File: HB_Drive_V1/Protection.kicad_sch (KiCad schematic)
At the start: 48 parts, among them J701 Conn_02x02_Odd_Even, J702 Conn_02x02_Odd_Even, SW701 PTS636SL43SMTRLFS, SW704 PTS636SL43SMTRLFS, U402 74LS08, U701 74AUC2G02, U702 74LS32, U703 TL082, U704 TL082, U705 LM311

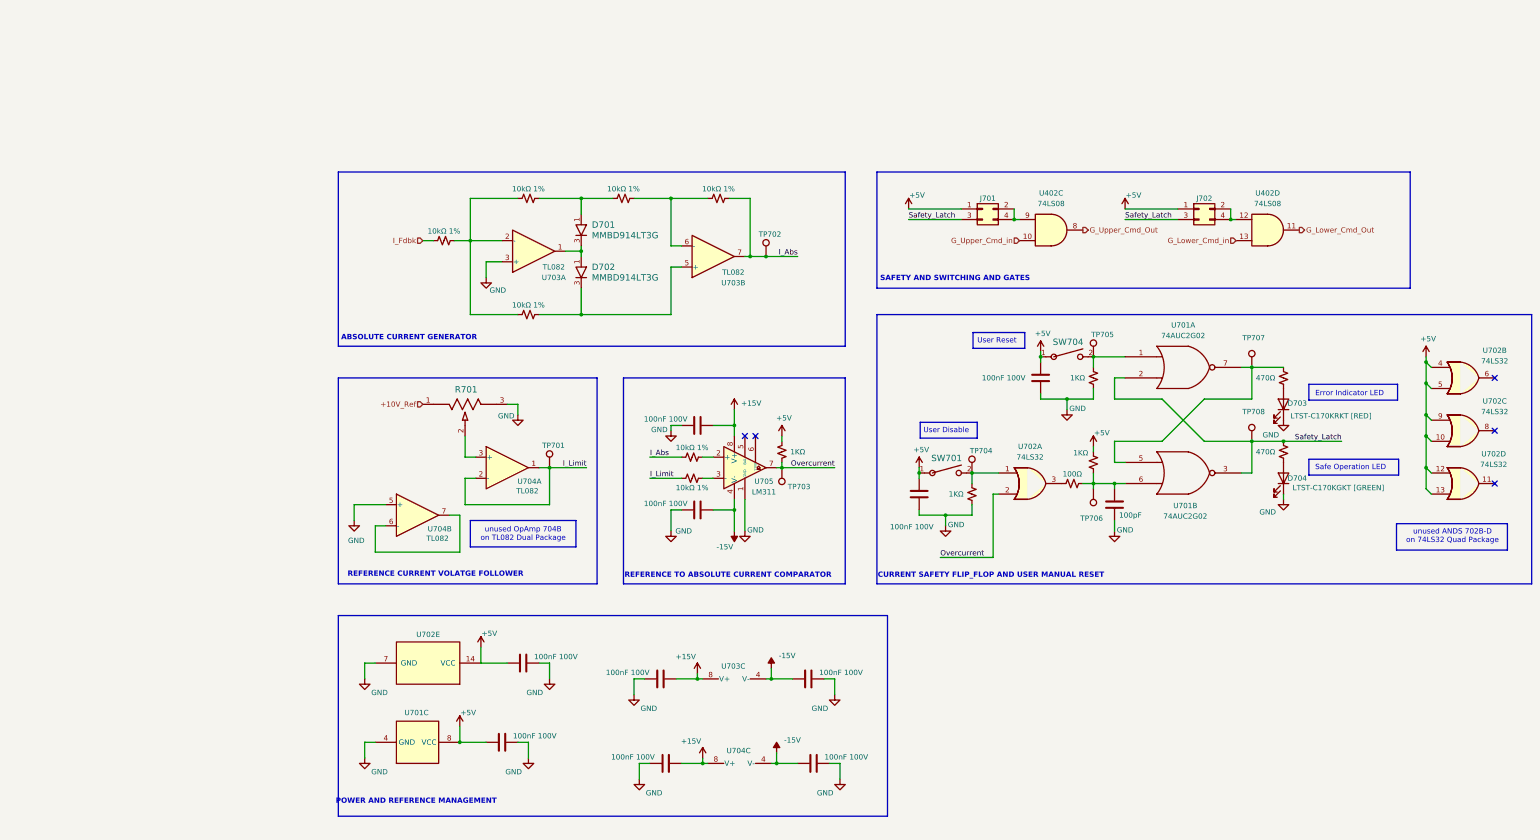
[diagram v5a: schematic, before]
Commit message: Annotates Schematic! Fixes REV1 wiring swaps and replaces buffer
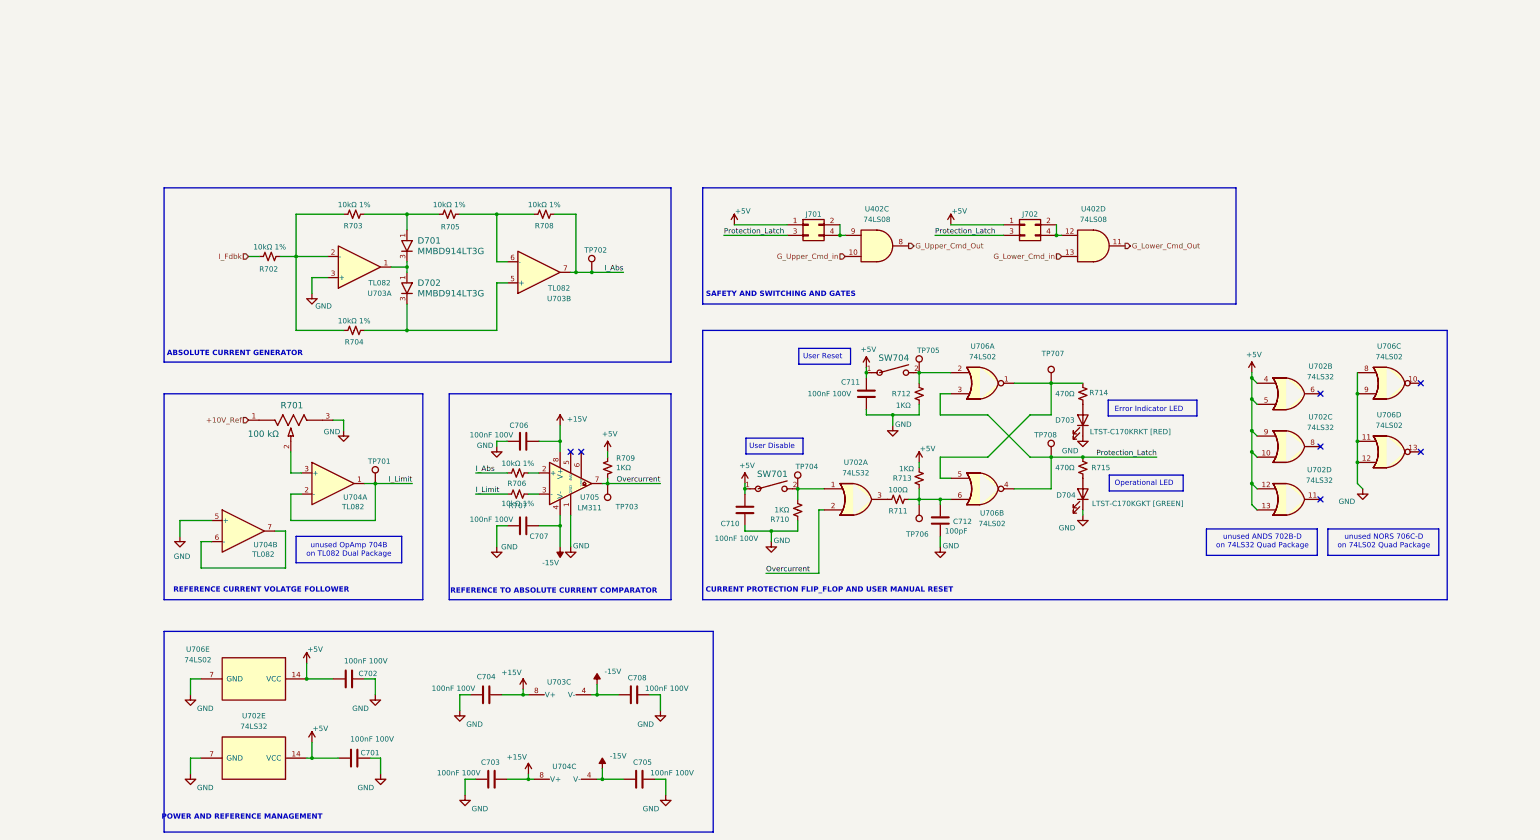
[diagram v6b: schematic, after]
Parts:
- removed U701: 74AUC2G02, Package_SO:VSSOP-8_2.3x2mm_P0.5mm, symbol 74xGxx:74AUC2G02
- added U706: 74LS02, Package_SO:SOIC-14_3.9x8.7mm_P1.27mm, symbol 74xx:74LS02
- D701, D702: footprint SOT-23_ONS -> MMBD914LT3G:SOT-23_ONS
- R701: value PV36W104C01B00 -> 100 kΩ
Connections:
- net +5V: now also U706.14 (VCC)
- net GND: now also U706.11, U706.12, U706.7 (GND), U706.8, U706.9
- net at C712.2, R711.2, R713.1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: now also U706.6
- net at R712.2, SW704.2, TP705.1: now also U706.2
- net at R714.2, TP707.1: now also U706.1, U706.5
- net Safety_Latch renamed Protection_Latch
- net Protection_Latch: now also U706.3, U706.4
- no-connect marks 5 -> 7
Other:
- note added: "CURRENT PROTECTION FLIP_FLOP AND USER MANUAL RESET"
- note added: "Operational LED"
- note added: "unused NORS 706C-D on 74LS02 Quad Package"
- note removed: "CURRENT SAFETY FLIP_FLOP AND USER MANUAL RESET"
- note removed: "Safe Operation LED"
- moved on the sheet: D701, D702, D703, D704, J701, J702, R701, SW701, SW704, TP701, TP702, TP703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

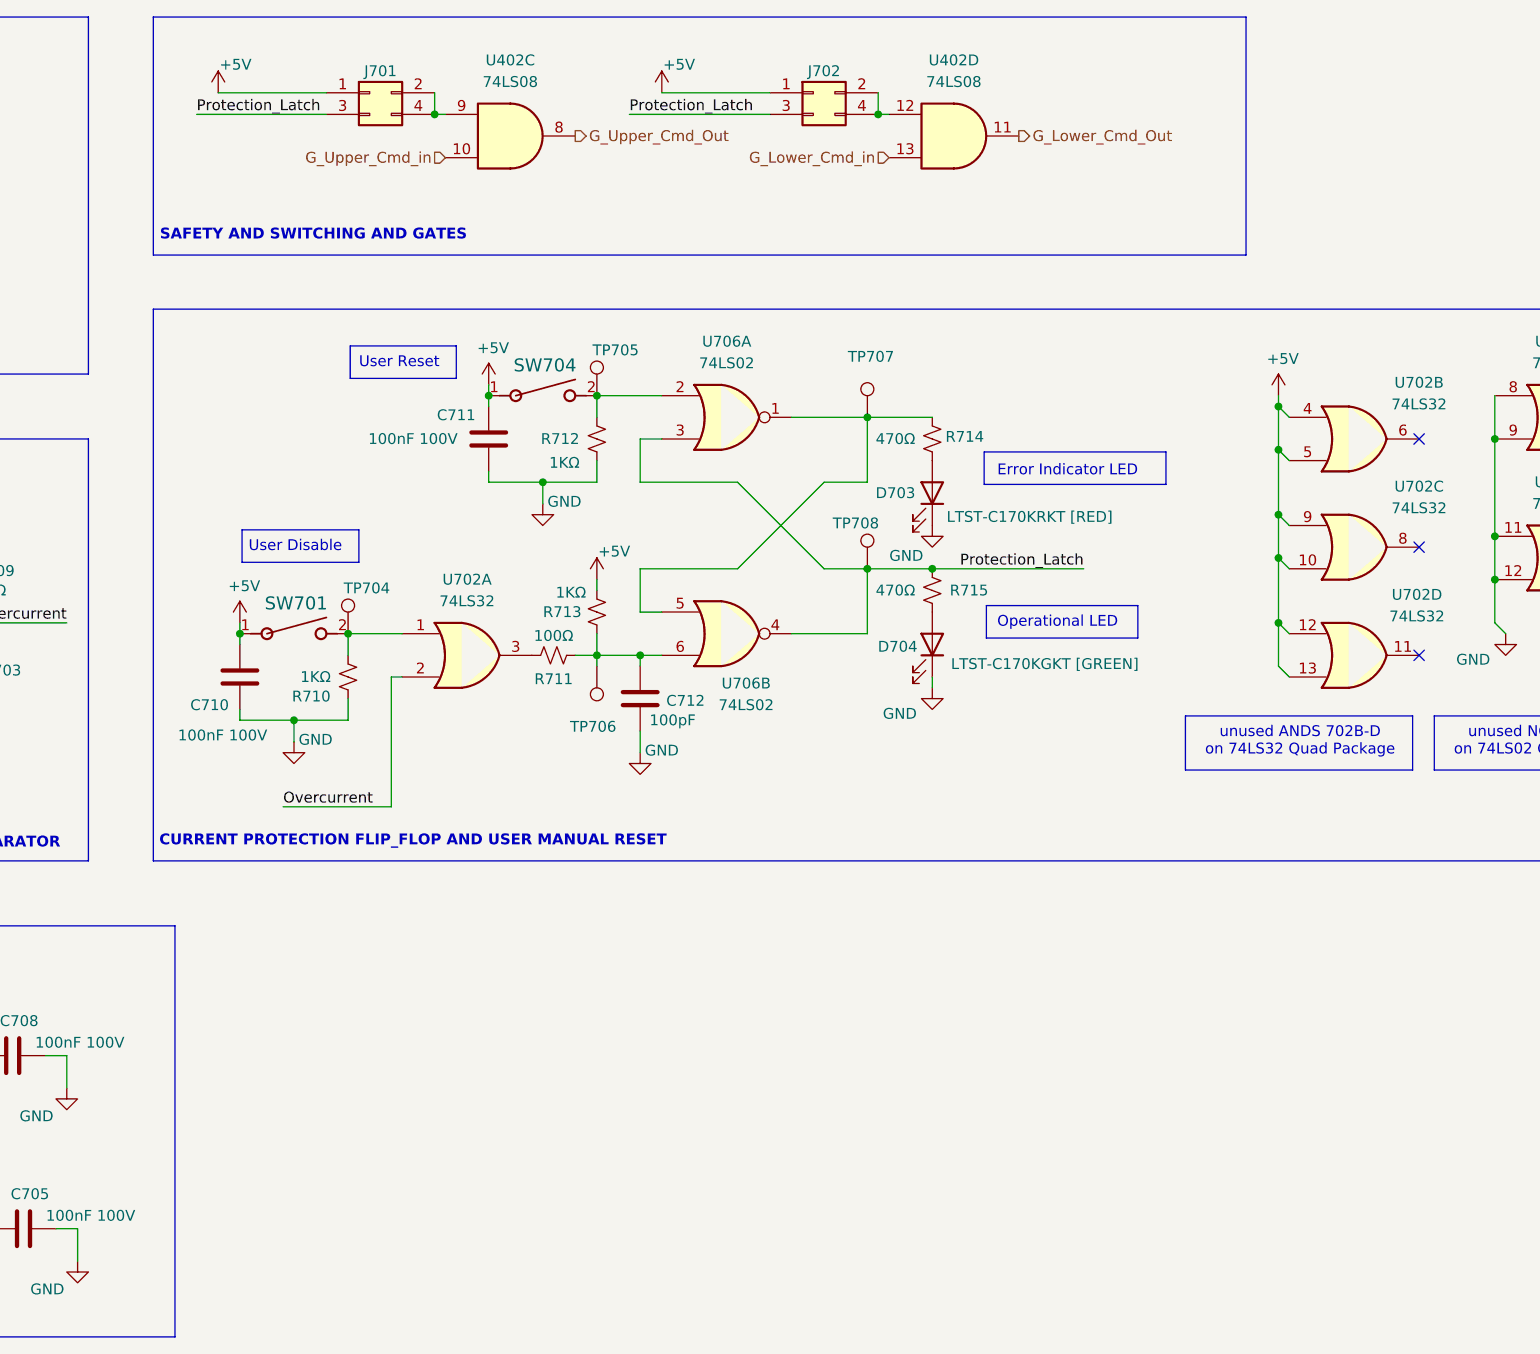
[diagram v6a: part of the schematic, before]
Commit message: Moves Ports and adds level shifter
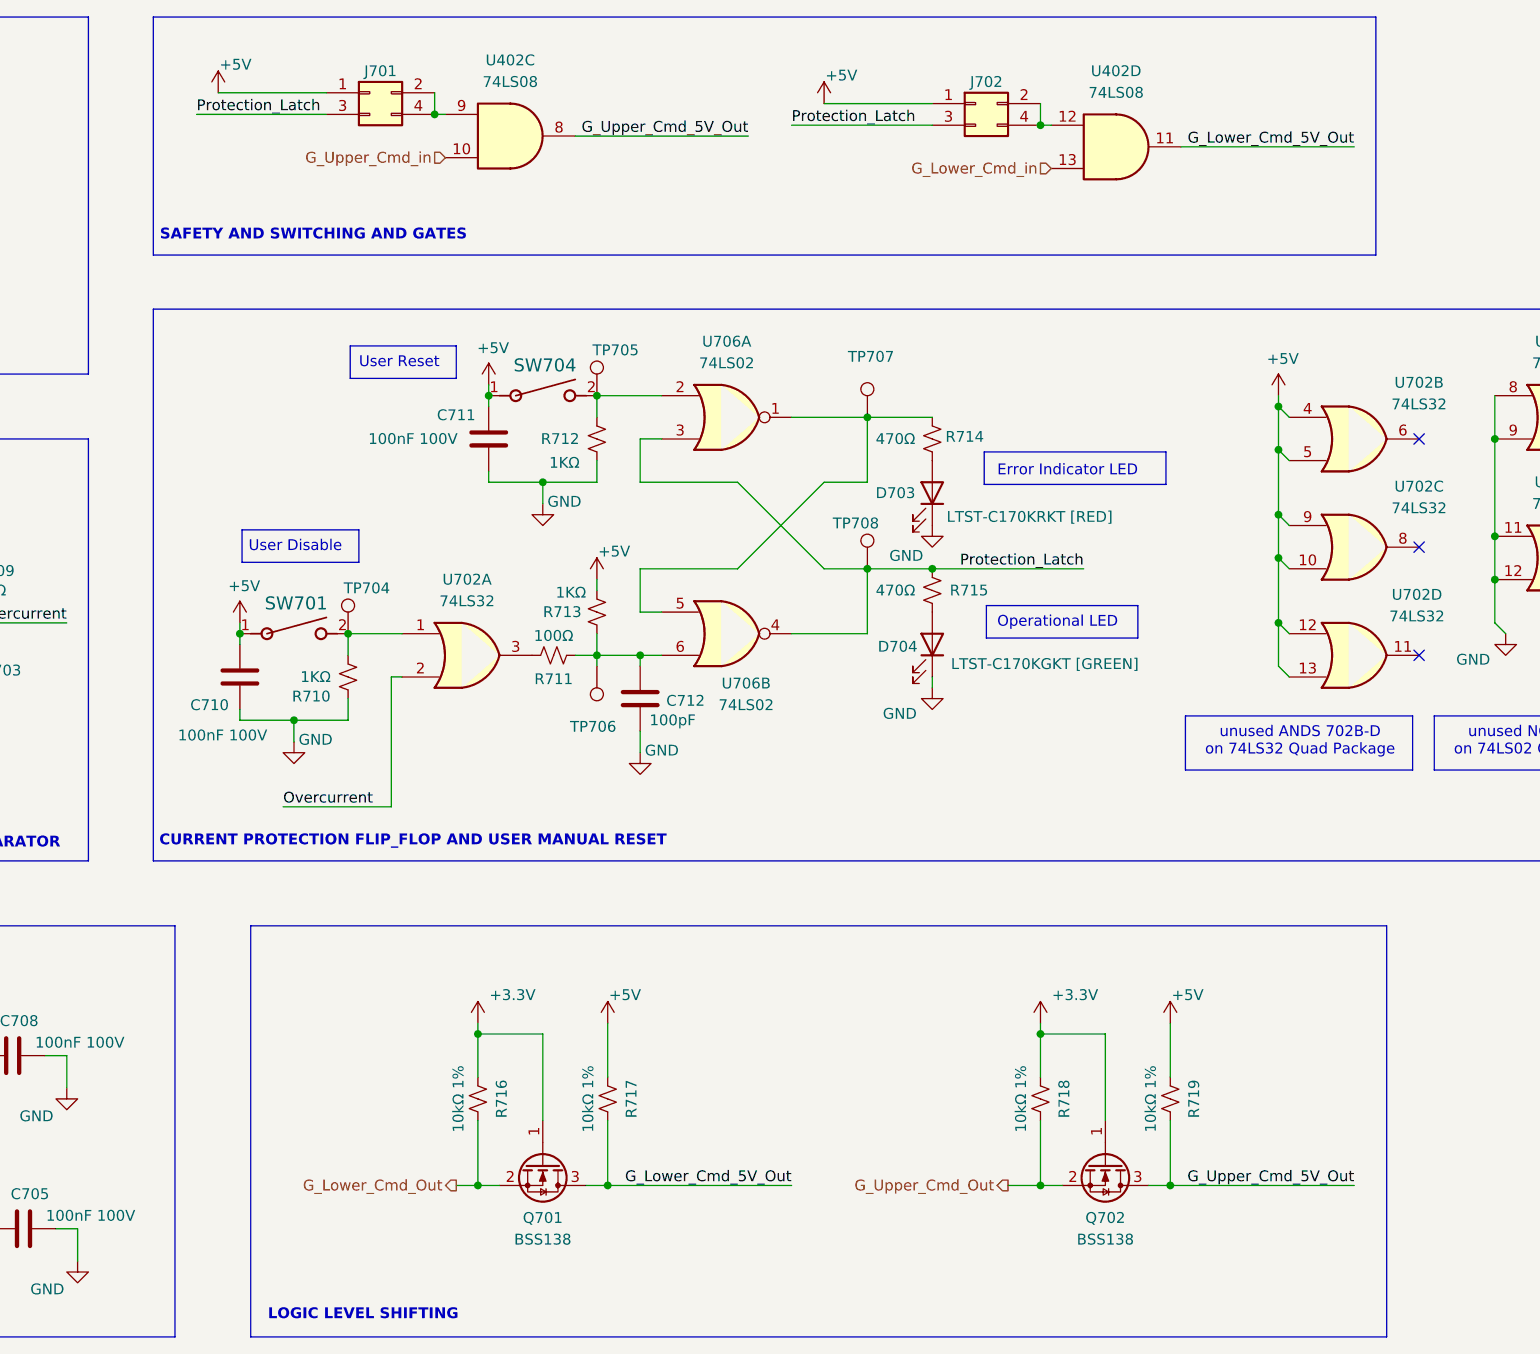
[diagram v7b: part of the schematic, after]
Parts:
- added Q701, Q702: BSS138, Package_TO_SOT_SMD:SOT-23, symbol Transistor_FET:BSS138
- added R716, R717, R718, R719: 10kΩ 1%, Resistor_SMD:R_0603_1608Metric_Pad0.98x0.95mm_HandSolder, symbol Device:R_Small_US
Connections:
- net +5V: now also R717.2, R719.2
- net G_Lower_Cmd_Out: now also Q701.2 (S), R716.1; no longer U402.11
- net G_Upper_Cmd_Out: now also Q702.2 (S), R718.1; no longer U402.8
- new net +3.3V: Q701.1 (G), Q702.1 (G), R716.2, R718.2
- new net G_Lower_Cmd_5V_Out: Q701.3 (D), R717.1, U402.11
- new net G_Upper_Cmd_5V_Out: Q702.3 (D), R719.1, U402.8
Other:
- note added: "LOGIC LEVEL SHIFTING"
- moved on the sheet: J702, U402D

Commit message: Brings everything up to latest copy on my computer
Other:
- company: (none) -> UW Madison, WEMPEC
- title: (none) -> HB Drive V3
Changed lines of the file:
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@@
 	(generator_version "10.0")
 	(paper "A3")
+	(title_block
+		(title "HB Drive V3")
+		(date "2026-09-08")
+		(company "UW Madison, WEMPEC")
+	)
 	(rectangle
 		(start 304.038 145.542)
